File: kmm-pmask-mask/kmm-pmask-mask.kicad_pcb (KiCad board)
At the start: 2 copper layers, 90.4 x 109 mm, 68 parts, among them J1 F31L-1A7H1-11030, U1 MS5611-01BA, U10 MAX30101EFD_T, U11 SHT40-AD1B-R3, U12 SHT40-AD1B-R3, U13 TMP117MAIDRVR, U14 TMP117MAIDRVR, U15 TCA9546APW, U2 MAX30101EFD_T, U3 SHT40-AD1B-R3, U4 TMP117MAIDRVR, U5 MS5611-01BA, U6 MS5611-01BA, U7 MS5611-01BA, U8 MAX30101EFD_T, U9 MAX30101EFD_T

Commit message: track cleanup
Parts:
- TP1, TP11, TP12, TP13, TP14, TP15, TP16, TP17, TP2, TP3, TP4, TP5, TP6, TP7, TP8: footprint TestPoint:TestPoint_Pad_D1.5mm -> TestPoint:TestPoint_Pad_D1.0mm; moved to B.Cu
- TP10, TP9: footprint TestPoint:TestPoint_Pad_D1.5mm -> TestPoint:TestPoint_Pad_D1.0mm
- moved TP14 104.5 mm to (41.5, 107.0), turned to 180 degrees
- moved TP2 99.4 mm to (40.0, 108.8), turned to 180 degrees
- moved TP1 96.7 mm to (43.8, 108.2), turned to 180 degrees
- moved TP13 93.8 mm to (76.0, 145.5), turned to 180 degrees
- moved TP5 92.4 mm to (58.0, 143.5), turned to 180 degrees
- moved TP17 91.4 mm to (67.0, 144.8), turned to 180 degrees
- moved TP6 91.4 mm to (55.5, 140.8), turned to 180 degrees
- moved TP11 77.1 mm to (82.0, 145.5), turned to 180 degrees
- moved TP9 72.0 mm to (77.6, 51.2)
- moved TP12 71.4 mm to (86.5, 145.5), turned to 180 degrees
- moved TP10 70.2 mm to (80.0, 54.2)
- moved TP15 66.4 mm to (77.4, 79.8), turned to 180 degrees
- moved TP4 64.6 mm to (72.6, 79.8), turned to 180 degrees
- moved TP3 61.7 mm to (75.0, 79.8), turned to 180 degrees
- moved TP8 41.9 mm to (105.8, 108.2), turned to 180 degrees
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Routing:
- net GND: track 59.7 -> 62.6 mm, vias 65 -> 70
- net /I2C_M_SCL: track 9.05 -> 11.3 mm
- net /I2C0_SCL: track 74.4 -> 76.6 mm, vias 2 -> 3
- net /I2C3_SCL: track 73.0 -> 75.0 mm, vias 2 -> 3
- net /I2C2_SDA: track 155.5 -> 157.5 mm, vias 0 -> 1
- net /I2C1_SCL: track 27.8 -> 29.5 mm, vias 0 -> 1
- net /I2C1_SDA: track 29.4 -> 31.1 mm, vias 0 -> 1
- net +3.3V: track 345.1 -> 346.7 mm, vias 19 -> 20
- net /I2C2_SCL: track 154.8 -> 156.3 mm, vias 2 -> 3
- net +5V: track 260.6 -> 262.1 mm
- net /I2C3_SDA: track 72.5 -> 73.9 mm, vias 2 -> 3
- net /I2C0_SDA: track 80.2 -> 81.5 mm, vias 2 -> 3
- net /I2C_M_SDA: track 11.0 -> 12.2 mm
- net +1.8V: track 243.6 -> 244.1 mm

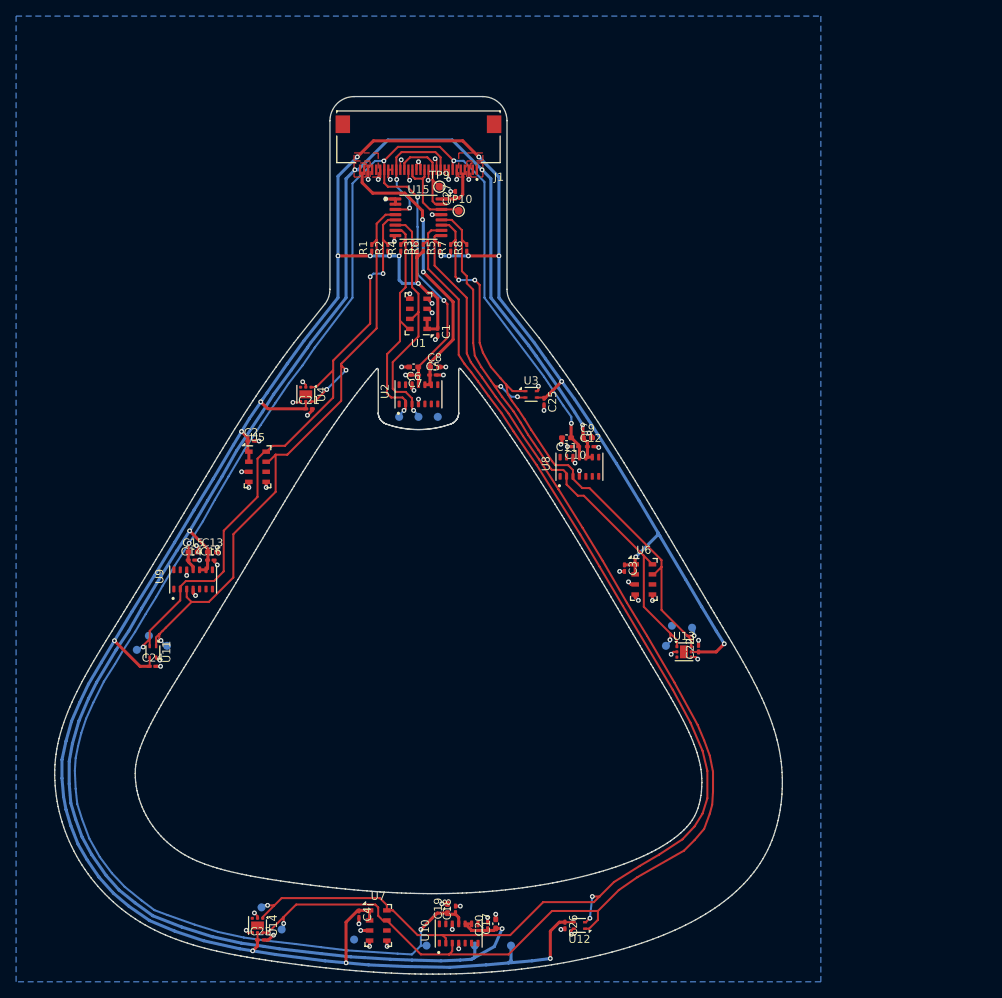
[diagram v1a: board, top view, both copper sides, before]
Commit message: Silkscreen cleanup
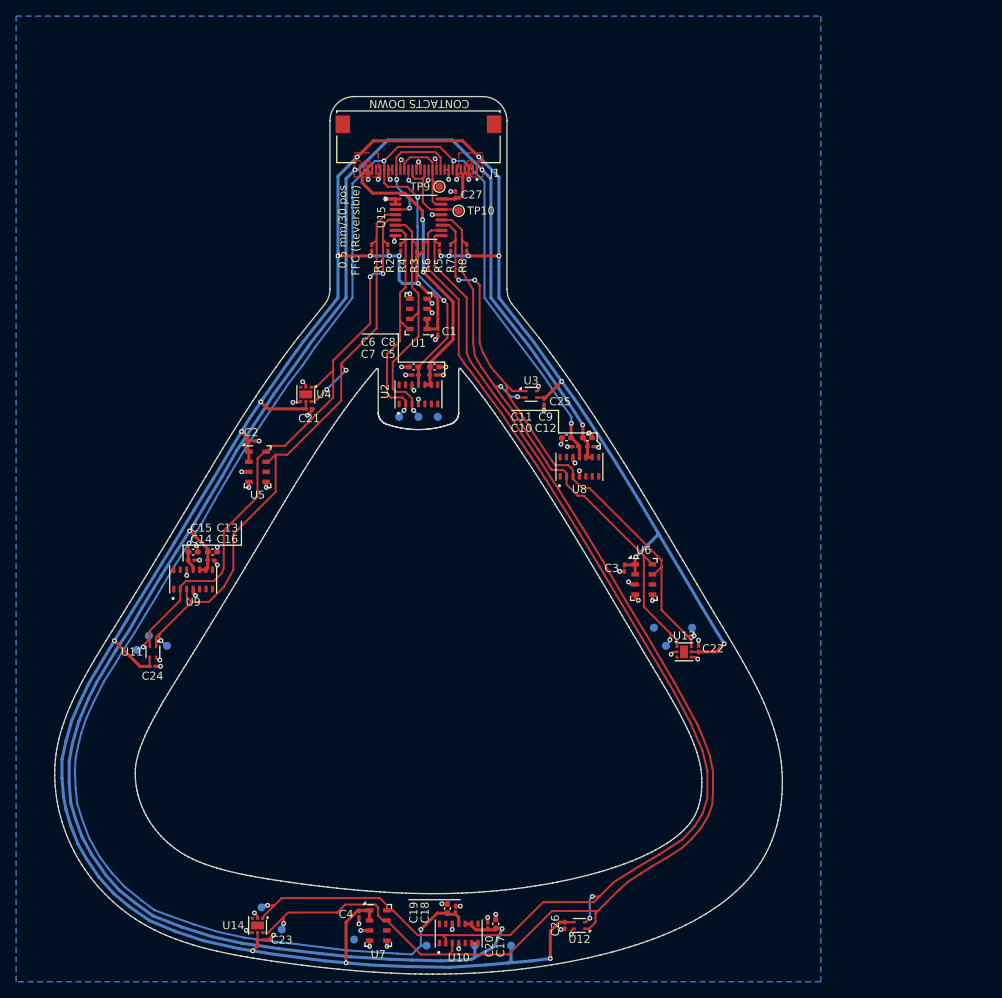
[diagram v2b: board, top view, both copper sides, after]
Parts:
- added G***: LOGO, kmm-pmask:GRAPHIC_KAMOAMOA, B.Cu at (84.0, 70.0)
- added G***: LOGO, kmm-pmask:GRAPHIC_PIMAN_PCB, B.Cu at (75.0, 69.0)
- added G***: LOGO, kmm-pmask:GRAPHIC_GT_VERT, B.Cu at (66.0, 70.0)
- moved TP15 65.8 mm to (67.0, 144.8)
- moved TP16 65.0 mm to (41.5, 107.0)
- moved TP17 53.8 mm to (104.2, 106.0)
- moved TP14 45.0 mm to (77.4, 79.8)
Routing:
- net +5V: track 262.1 -> 261.3 mm
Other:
- board text added: "0.5 mm/30 pos FFC (Reversible)"
- board text added: "CONTACTS DOWN"
- board text added: "STIFFENER"
- board text added: "Sensing Mask Insert Ka Moamoa Lab Rev 2.0"

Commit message: Add fiducials, missing 3D
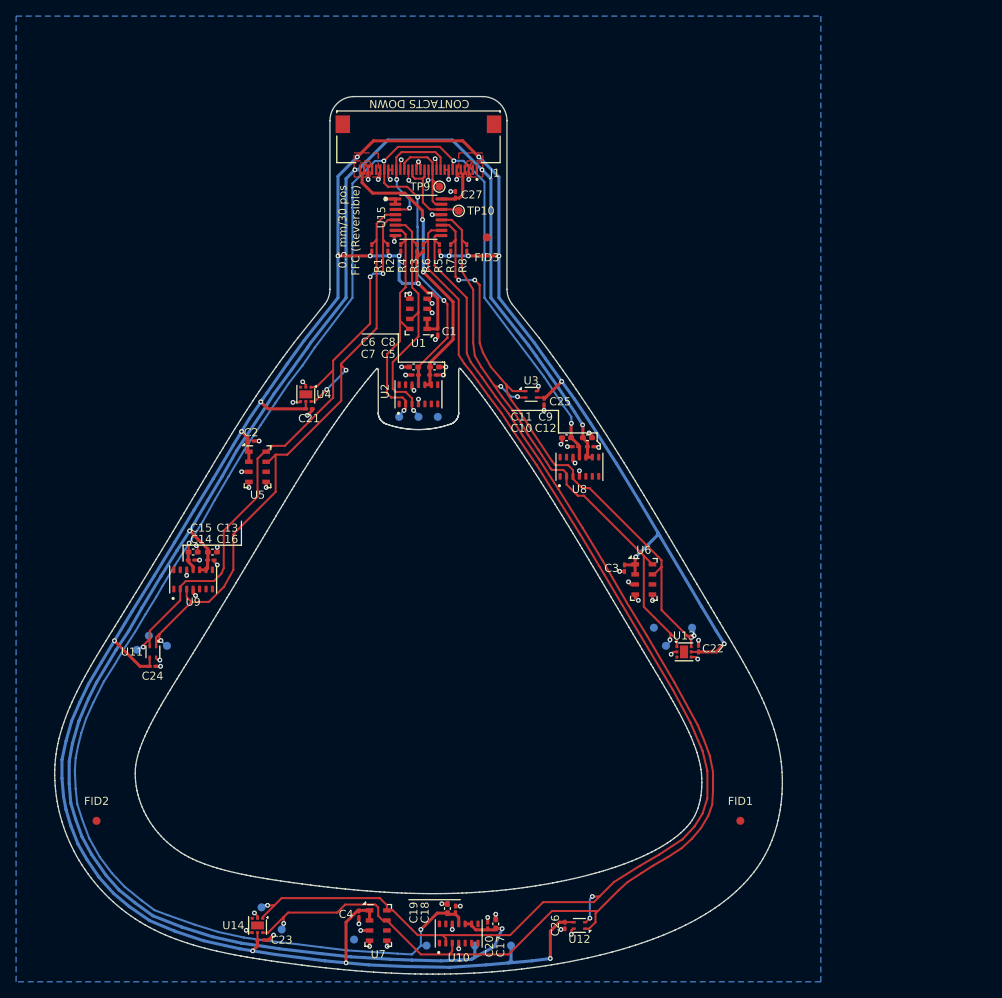
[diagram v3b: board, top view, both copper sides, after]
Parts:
- added FID1: Fiducial, Fiducial:Fiducial_1mm_Mask3mm, F.Cu at (115.0, 130.0)
- added FID2: Fiducial, Fiducial:Fiducial_1mm_Mask3mm, F.Cu at (35.0, 130.0)
- added FID3: Fiducial, Fiducial:Fiducial_1mm_Mask3mm, F.Cu at (83.5, 57.5)
- moved G*** 1.00 mm to (75.0, 70.0)

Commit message: Production Candidate 1
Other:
- board text added: "STIFFENER PI (Polyimide) 0.2mm"
- board text removed: "STIFFENER PI (Polyamide) 0.2mm"
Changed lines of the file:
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@@
 	)
 	(gr_line
+		(start 25 45)
+		(end 125 45)
+		(stroke
+			(width 0.1)
+			(type dash)
+		)
+		(layer "Dwgs.User")
+	)
+	(gr_line
 		(start 25 55)
 		(end 125 55)
@@
 		)
 	)
-	(gr_text "STIFFENER\nPI (Polyamide) 0.2mm"
+	(gr_text "STIFFENER\nPI (Polyimide) 0.2mm"
 		(at 91 40 0)
 		(layer "User.2")
@@
 		)
 	)
+	(gr_text_box "Designed for JLCPCB Flex Process\n\nSpecifications:\nDielectric Thickness: 25 μm \nPCB Thickness: 0.12 mm\nCopper Type: Electro-deposited\nSurface Finish: ENIG\nGold Thickness: 1 U{dblquote}\nOuter Copper Weight: 0.5 oz/ft^{2}\nStiffener: Yes, PI (Polyimide) 0.2 mm\nEMI shielding: No\nCutting Method: Laser\nSilkscreen on Stiffener: No\n\nRemark:\nStiffener geometry specified on separate layer."
+		(start 130 30)
+		(end 170 60)
+		(margins 1.0025 1.0025 1.0025 1.0025)
+		(layer "Cmts.User")
+		(effects
+			(font
+				(size 1 1)
+				(thickness 0.15)
+			)
+			(justify left top)
+		)
+		(border yes)
+		(stroke
+			(width 0.1)
+			(type solid)
+		)
+		(knockout no)
+	)
+	(gr_text_box "Remarks on Assembly:\n\nIt is recommended to pre-bake this board before assembly and reflow.\nUse low-temp solder paste (Sn42/Bi58) if possible. Otherwise reflow temperature must not exceed 260 °C.\nThree fiducial marks are provided but automated assembly is not recommended without addition of a fixture."
+		(start 130 65)
+		(end 170 85)
+		(margins 1.0025 1.0025 1.0025 1.0025)
+		(layer "Cmts.User")
+		(effects
+			(font
+				(size 1 1)
+				(thickness 0.15)
+			)
+			(justify left top)
+		)
+		(border yes)
+		(stroke
+			(width 0.1)
+			(type solid)
+		)
+		(knockout no)
+	)
 	(dimension
 		(type orthogonal)
@@
 			(layer "Dwgs.User")
 			(effects
+				(font
+					(size 1 1)
+					(thickness 0.15)
+				)
+			)
+		)
+	)
+	(dimension
+		(type orthogonal)
+		(layer "Dwgs.User")
+		(pts
+			(xy 125 55) (xy 125 45)
+		)
+		(height 0)
+		(orientation 1)
+		(format
+			(prefix "")
+			(suffix "")
+			(units 3)
+			(units_format 0)
+			(precision 4)
+			(suppress_zeroes yes)
+		)
+		(style
+			(thickness 0.1)
+			(arrow_length 1.27)
+			(text_position_mode 0)
+			(arrow_direction outward)
+			(extension_height 0.58642)
+			(extension_offset 0.5)
+			(keep_text_aligned yes)
+		)
+		(gr_text "10"
+			(at 123.85 50 90)
+			(layer "Dwgs.User")
+			(effects

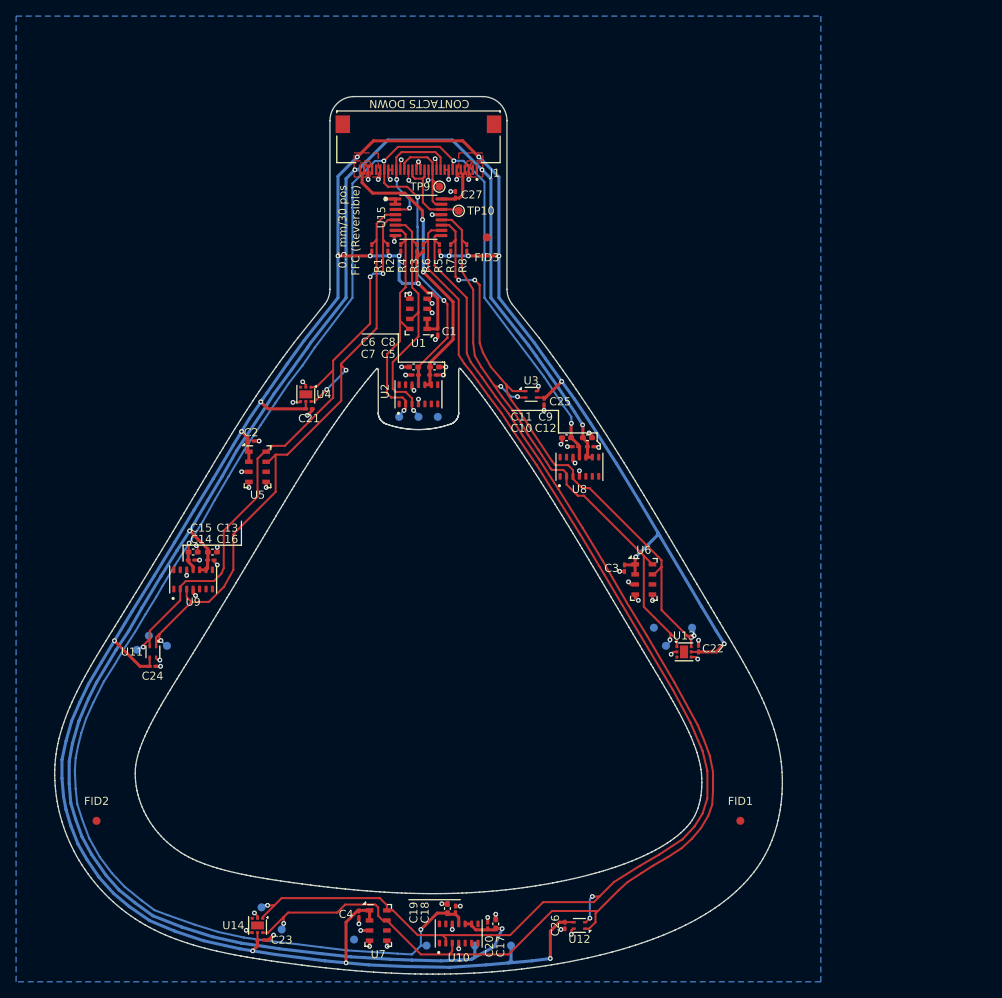
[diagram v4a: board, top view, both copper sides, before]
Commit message: Add pull-ups for unused interrupt line, just in case
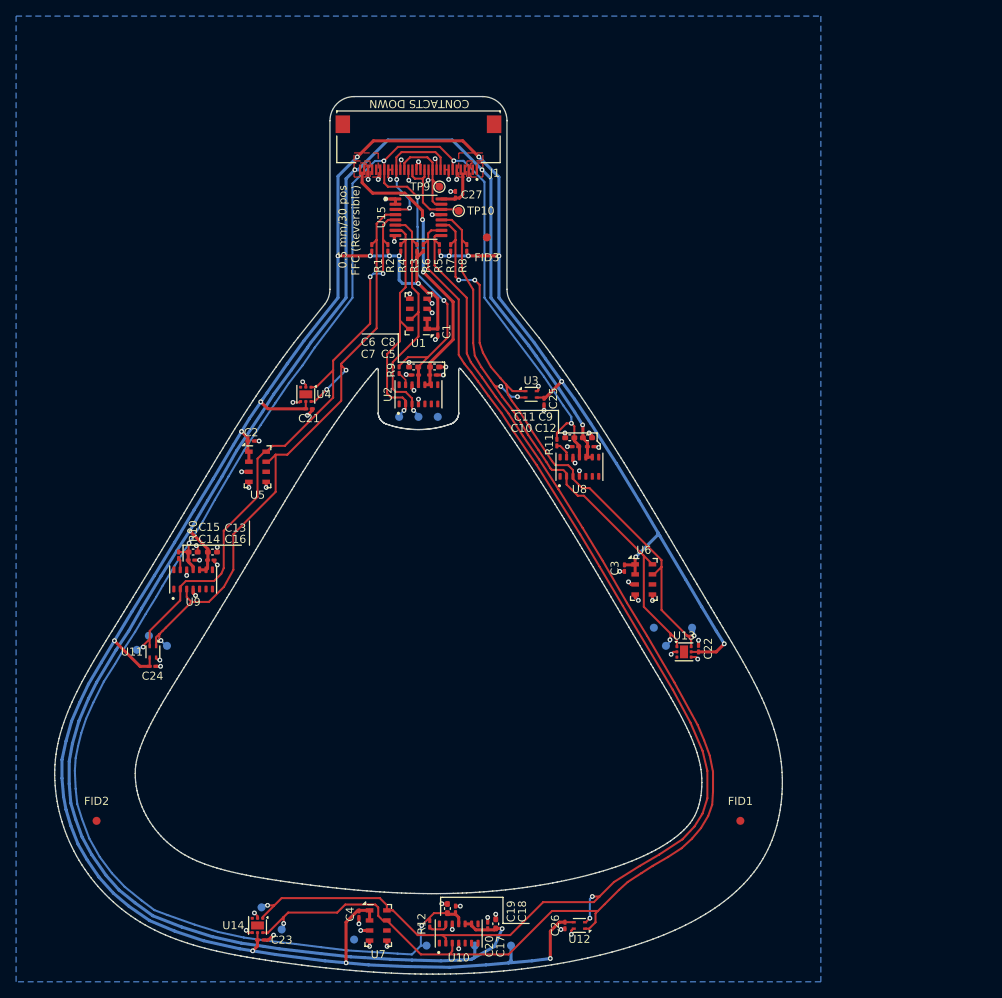
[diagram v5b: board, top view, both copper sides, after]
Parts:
- added R10: 4.7k, Resistor_SMD:R_0201_0603Metric_Pad0.64x0.40mm_HandSolder, F.Cu at (45.2, 97.0)
- added R11: 4.7k, Resistor_SMD:R_0201_0603Metric_Pad0.64x0.40mm_HandSolder, F.Cu at (92.2, 83.0)
- added R12: 4.7k, Resistor_SMD:R_0201_0603Metric_Pad0.64x0.40mm_HandSolder, F.Cu at (76.4, 142.8)
- added R9: 4.7k, Resistor_SMD:R_0201_0603Metric_Pad0.64x0.40mm_HandSolder, F.Cu at (72.6, 74.0)
- moved C11 0.40 mm to (93.8, 82.4)
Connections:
- U10 pad 13: unconnected-(U10-~{INT}-Pad13) -> Net-(U10-~{INT})
- U2 pad 13: unconnected-(U2-~{INT}-Pad13) -> Net-(U2-~{INT})
- U8 pad 13: unconnected-(U8-~{INT}-Pad13) -> Net-(U8-~{INT})
- U9 pad 13: unconnected-(U9-~{INT}-Pad13) -> Net-(U9-~{INT})
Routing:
- net +1.8V: track 244.1 -> 252.9 mm
- net Net-(U10-~{INT}): track 0.00 -> 2.64 mm
- net Net-(U8-~{INT}): track 0.00 -> 2.13 mm
- net Net-(U2-~{INT}): track 0.00 -> 1.73 mm
- net Net-(U9-~{INT}): track 0.00 -> 1.48 mm
- net GND: track 62.6 -> 61.9 mm

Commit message: Production Candidate 2
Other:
- board text added: "Sensing Mask Insert Rev 2.0"
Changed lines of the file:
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@@
 		(tags "WSON NoLead")
 		(property "Reference" "U4"
-			(at 0 -2.25 180)
+			(at 0 -2.2 270)
 			(layer "F.SilkS")
 			(effects
@@
 		(tags "DFN NoLead")
 		(property "Reference" "U3"
-			(at 0 -1.7 0)
+			(at -2.25 0 90)
 			(layer "F.SilkS")
 			(effects
@@
 		(tags "capacitor handsolder")
 		(property "Reference" "C1"
-			(at 0 -1.1 270)
+			(at 1.8 0 270)
 			(layer "F.SilkS")
 			(effects
@@
 		(layer "User.2")
 	)
+	(gr_text "Sensing\nMask Insert\nRev 2.0"
+		(at 84 70.5 0)
+		(layer "F.SilkS")
+		(effects
+			(font
+				(size 1 1)
+				(thickness 0.15)
+			)
+		)
+	)
 	(gr_text "0.5 mm/30 pos \nFFC (Reversible)"
